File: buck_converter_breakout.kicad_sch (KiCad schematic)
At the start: 29 parts, among them Q1 Q_NPN, U1 MIC24066T-E/QNA

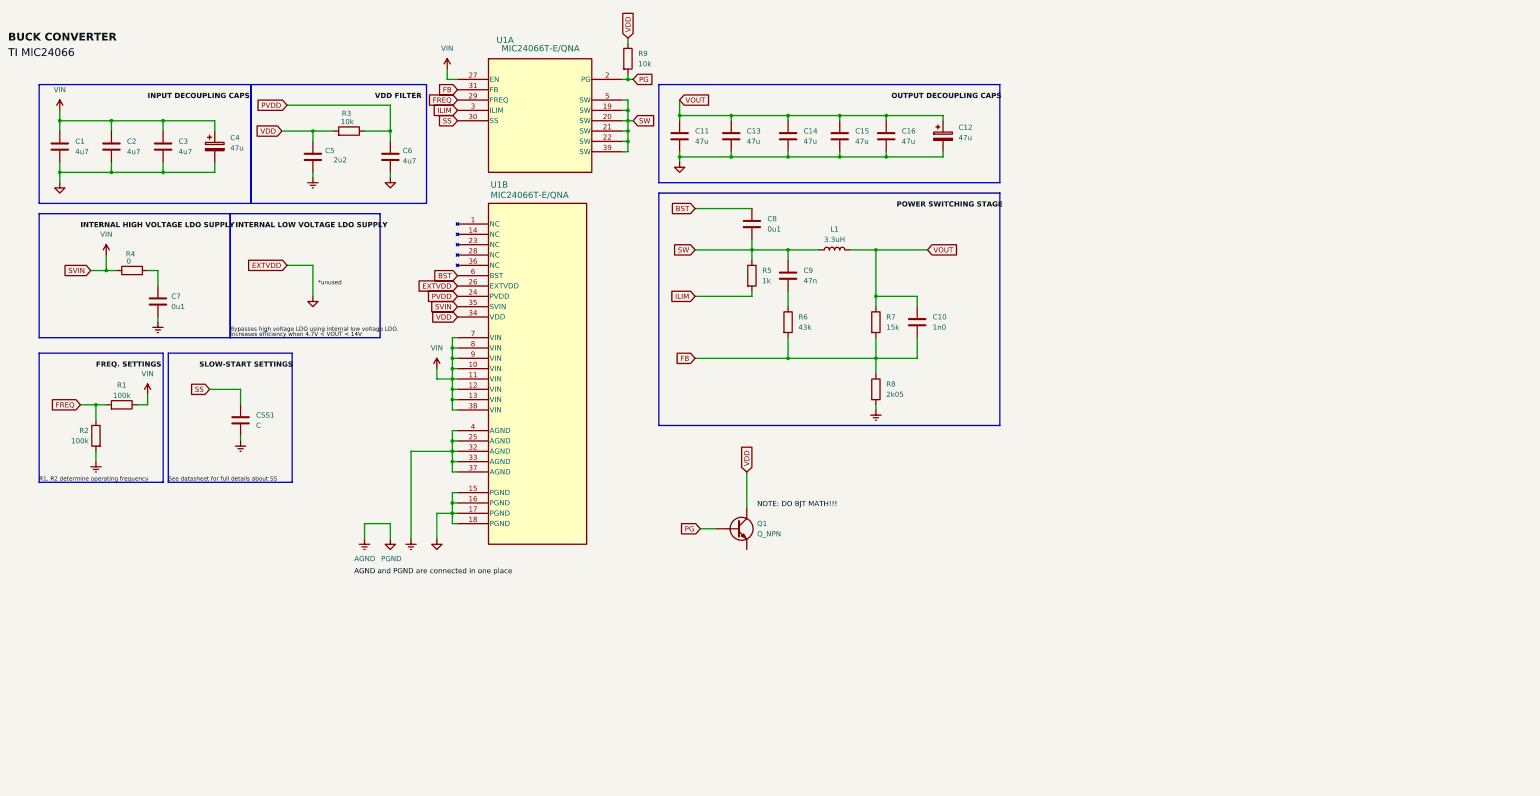
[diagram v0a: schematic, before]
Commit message: added pg led, reverse polarity protection
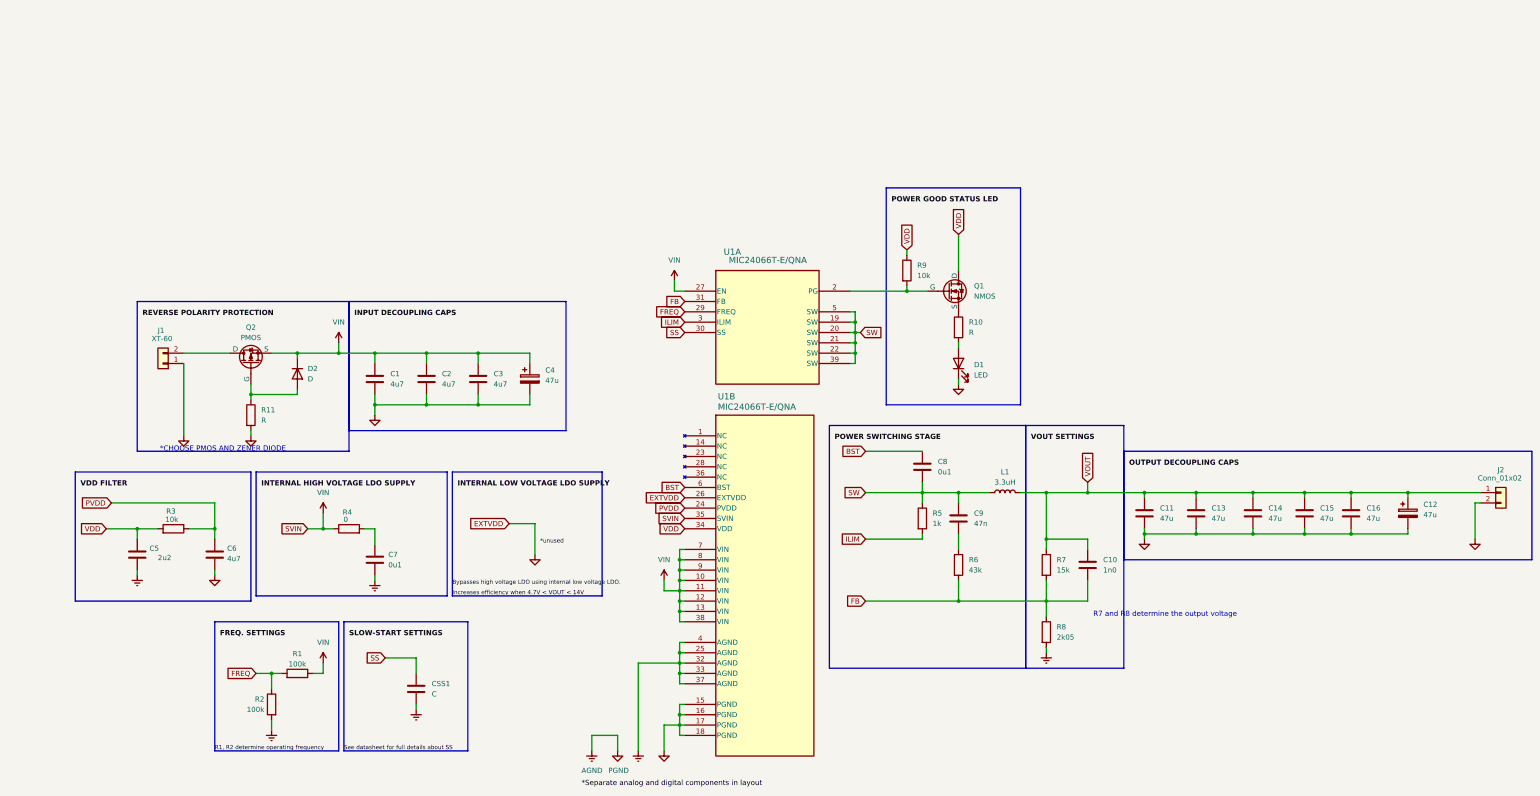
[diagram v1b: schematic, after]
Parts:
- removed Q1: Q_NPN, symbol Device:Q_NPN
- added D1: LED, symbol Device:LED
- added D2: D, symbol Device:D
- added J1: XT-60, symbol Connector_Generic:Conn_01x02
- added J2: Conn_01x02, symbol Connector_Generic:Conn_01x02
- added Q1: NMOS, symbol Simulation_SPICE:NMOS
- added Q2: PMOS, symbol Simulation_SPICE:PMOS
- added R10, R11: R, symbol Device:R
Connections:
- net AGND: now also D1.1 (K), J1.1 (Pin_1), J2.2 (Pin_2), R11.2
- net VDD: now also Q1.1 (D)
- net VIN: now also D2.1 (K), Q2.3 (S)
- net VOUT: now also J2.1 (Pin_1)
- net PG: no longer names the net of R9.2, U1.2 (PG)
- net PG: now also Q1.2 (G)
- new net: D1.2 (A), R10.2
- new net: J1.2 (Pin_2), Q2.1 (D)
- new net: D2.2 (A), Q2.2 (G), R11.1
- new net: Q1.3 (S), R10.1
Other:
- note added: "*CHOOSE PMOS AND ZENER DIODE"
- note added: "R7 and R8 determine the output voltage"
- title: (none) -> 6S Lipo Battery Step Down Converter
- moved on the sheet: C1, C10, C11, C12, C13, C14, C15, C16, C2, C3, C4, C5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
